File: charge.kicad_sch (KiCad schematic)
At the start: 2 parts, among them U1 BQ24640RVAR

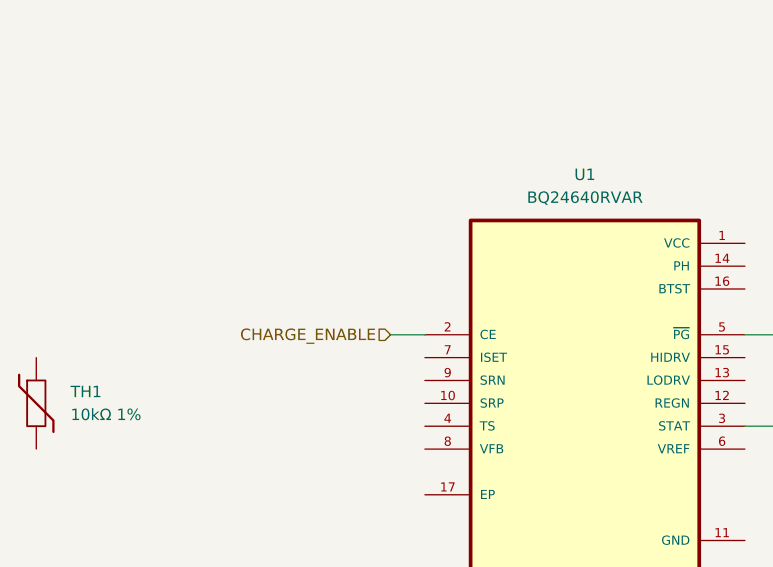
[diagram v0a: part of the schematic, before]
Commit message: Prefix all of the references so that the numbering is manageable across multiple circuits
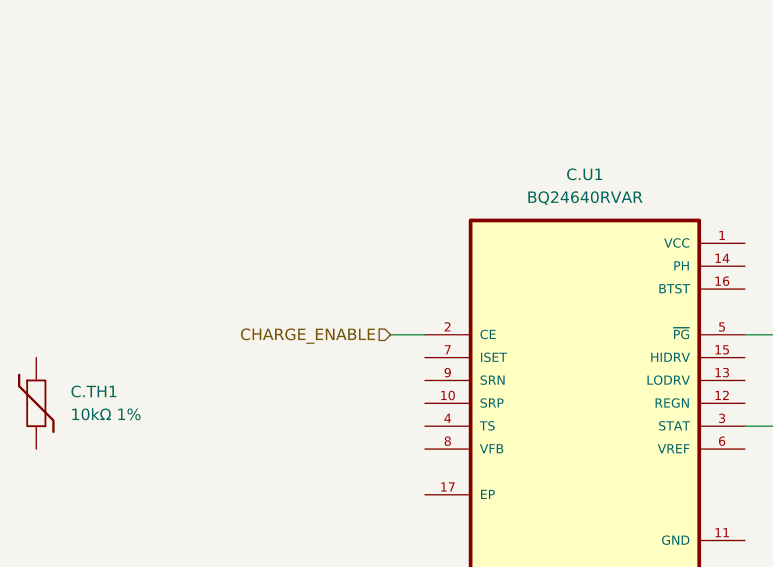
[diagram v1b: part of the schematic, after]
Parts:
- renumbered TH1 to C.TH1, U1 to C.U1
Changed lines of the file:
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@@
 		(dnp no)
 		(fields_autoplaced yes)
-		(property "Reference" "U1"
+		(property "Reference" "C.U1"
 			(at 74.93 39.37 0)
 			(effects
@@
 			(project ""
 				(path "/01e6e533-9ed1-4dde-bac5-1959ff8991e5/a1435003-e5d3-4de7-a692-f8e6f931526d"
-					(reference "U1")
+					(reference "C.U1")
 					(unit 1)
 				)
@@
 		(dnp no)
 		(fields_autoplaced yes)
-		(property "Reference" "TH1"
+		(property "Reference" "C.TH1"
 			(at 17.78 63.4999 0)
 			(effects
@@
 			(project "wireless-3v3-supercap"
 				(path "/01e6e533-9ed1-4dde-bac5-1959ff8991e5/a1435003-e5d3-4de7-a692-f8e6f931526d"
-					(reference "TH1")
+					(reference "C.TH1")
 					(unit 1)
 				)

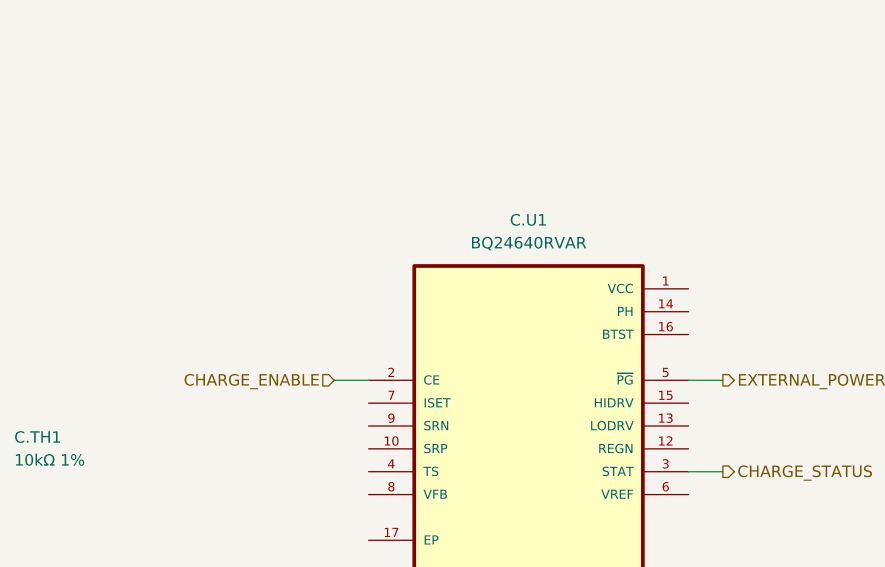
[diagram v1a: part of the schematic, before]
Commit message: Remove charge enable pin
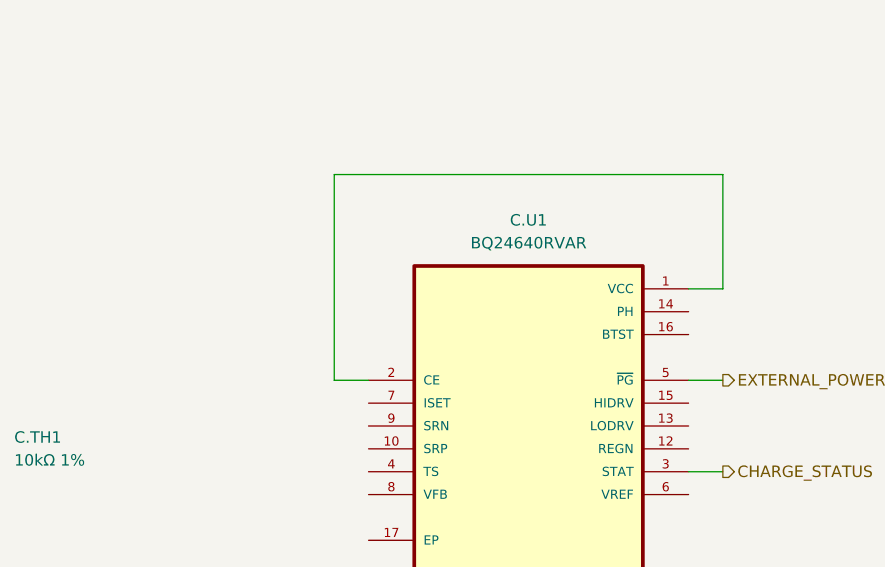
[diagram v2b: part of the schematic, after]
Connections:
- net CHARGE_ENABLE is gone; now on an unnamed net: C.U1.2 (CE)
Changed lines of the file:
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@@
+	(wire
+		(pts
+			(xy 53.34 34.29) (xy 96.52 34.29)
+		)
+		(stroke
+			(width 0)
+			(type default)
+		)
+	)
 	(wire
 		(pts
 			(xy 92.71 67.31) (xy 96.52 67.31)
+		)
+		(stroke
+			(width 0)
+			(type default)
+		)
+	)
+	(wire
+		(pts
+			(xy 96.52 46.99) (xy 92.71 46.99)
+		)
+		(stroke
+			(width 0)
+			(type default)
+		)
+	)
+	(wire
+		(pts
+			(xy 96.52 34.29) (xy 96.52 46.99)
+		)
+		(stroke
+			(width 0)
+			(type default)
+		)
+	)
+	(wire
+		(pts
+			(xy 53.34 57.15) (xy 53.34 34.29)
 		)
 		(stroke
@@
 		)
 	)
-	(hierarchical_label "CHARGE_ENABLE"
-		(shape input)
-		(at 53.34 57.15 180)
-		(effects
-			(font
-				(size 1.27 1.27)
-			)
-			(justify right)
-		)
-	)

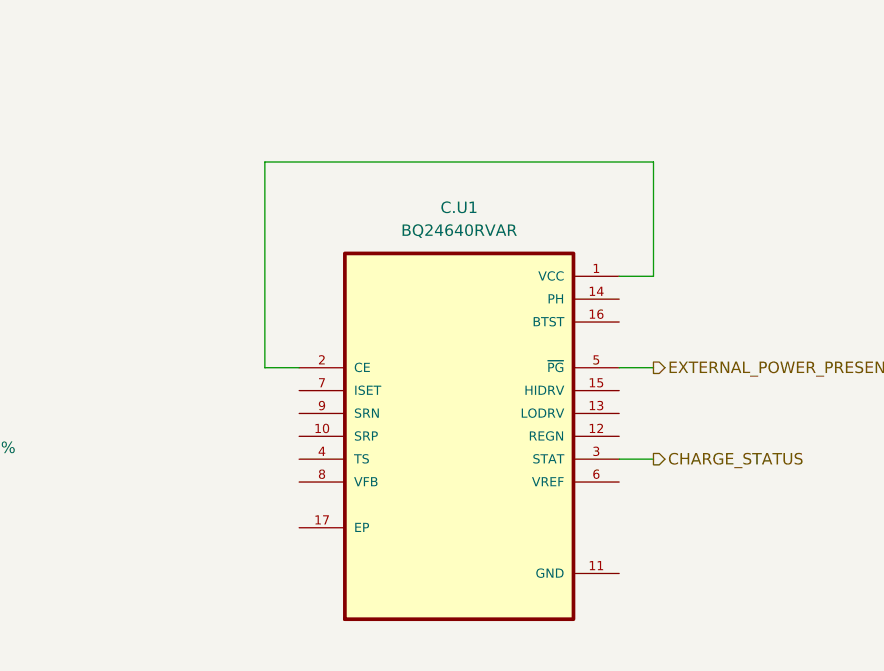
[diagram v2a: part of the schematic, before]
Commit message: Connect charger CE to VREF, not VCC
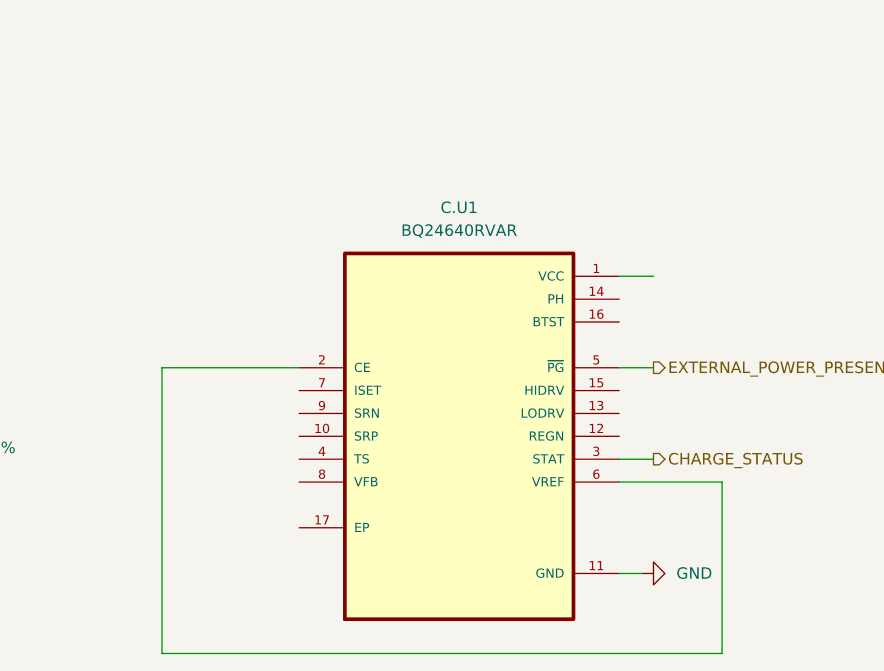
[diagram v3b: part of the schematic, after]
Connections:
- net at C.U1.1 (VCC): no longer C.U1.2 (CE)
- net GND: now reaches C.U1.11 (GND)
- net at C.U1.6 (VREF): now also C.U1.2 (CE)
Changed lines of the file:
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@@
 	(wire
 		(pts
-			(xy 53.34 34.29) (xy 96.52 34.29)
+			(xy 41.91 88.9) (xy 104.14 88.9)
+		)
+		(stroke
+			(width 0)
+			(type default)
+		)
+	)
+	(wire
+		(pts
+			(xy 104.14 69.85) (xy 92.71 69.85)
+		)
+		(stroke
+			(width 0)
+			(type default)
+		)
+	)
+	(wire
+		(pts
+			(xy 104.14 88.9) (xy 104.14 69.85)
 		)
 		(stroke
@@
 	(wire
 		(pts
+			(xy 41.91 57.15) (xy 41.91 88.9)
+		)
+		(stroke
+			(width 0)
+			(type default)
+		)
+	)
+	(wire
+		(pts
+			(xy 57.15 57.15) (xy 41.91 57.15)
+		)
+		(stroke
+			(width 0)
+			(type default)
+		)
+	)
+	(wire
+		(pts
 			(xy 96.52 46.99) (xy 92.71 46.99)
 		)
@@
 	(wire
 		(pts
-			(xy 96.52 34.29) (xy 96.52 46.99)
-		)
-		(stroke
-			(width 0)
-			(type default)
-		)
-	)
-	(wire
-		(pts
-			(xy 53.34 57.15) (xy 53.34 34.29)
-		)
-		(stroke
-			(width 0)
-			(type default)
-		)
-	)
-	(wire
-		(pts
-			(xy 53.34 57.15) (xy 57.15 57.15)
+			(xy 92.71 80.01) (xy 95.25 80.01)
 		)
 		(stroke
@@
 		)
 	)
+	(symbol
+		(lib_id "power:GND")
+		(at 95.25 80.01 90)
+		(unit 1)
+		(exclude_from_sim no)
+		(in_bom yes)
+		(on_board yes)
+		(dnp no)
+		(fields_autoplaced yes)
+		(property "Reference" "#PWR012"
+			(at 101.6 80.01 0)
+			(effects
+				(font
+					(size 1.27 1.27)
+				)
+				(hide yes)
+			)
+		)
+		(property "Value" "GND"
+			(at 99.06 80.0099 90)
+			(effects
+				(font
+					(size 1.27 1.27)
+				)
+				(justify right)
+			)
+		)
+		(property "Footprint" ""
+			(at 95.25 80.01 0)
+			(effects
+				(font
+					(size 1.27 1.27)
+				)
+				(hide yes)
+			)
+		)
+		(property "Datasheet" ""
+			(at 95.25 80.01 0)
+			(effects
+				(font
+					(size 1.27 1.27)
+				)
+				(hide yes)
+			)
+		)
+		(property "Description" "Power symbol creates a global label with name \"GND\" , ground"
+			(at 95.25 80.01 0)
+			(effects
+				(font
+					(size 1.27 1.27)
+				)
+				(hide yes)
+			)
+		)
+		(pin "1"
+		)
+		(instances
+			(project ""
+				(path "/01e6e533-9ed1-4dde-bac5-1959ff8991e5/a1435003-e5d3-4de7-a692-f8e6f931526d"
+					(reference "#PWR012")
+					(unit 1)
+				)
+			)
+		)
+	)

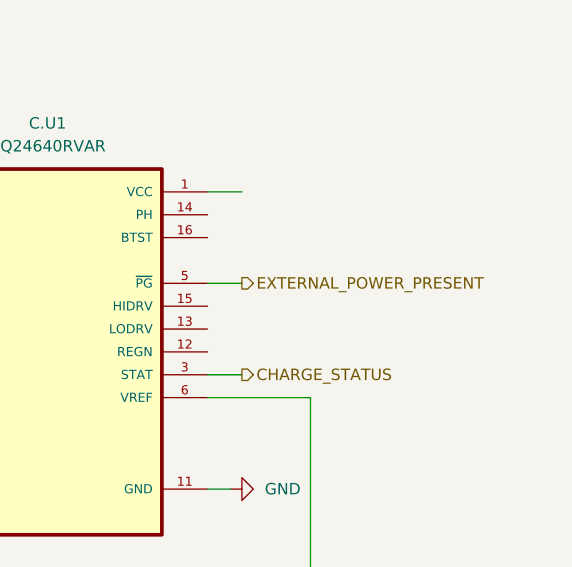
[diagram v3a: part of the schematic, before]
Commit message: Mark signals as active low
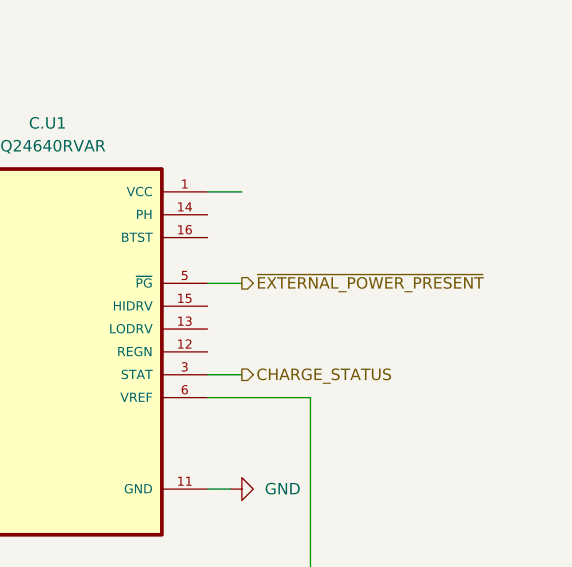
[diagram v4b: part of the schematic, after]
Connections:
- net EXTERNAL_POWER_PRESENT renamed ~{EXTERNAL_POWER_PRESENT}
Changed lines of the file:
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@@
 		)
 	)
-	(hierarchical_label "EXTERNAL_POWER_PRESENT"
+	(hierarchical_label "~{EXTERNAL_POWER_PRESENT}"
 		(shape output)
 		(at 96.52 57.15 0)

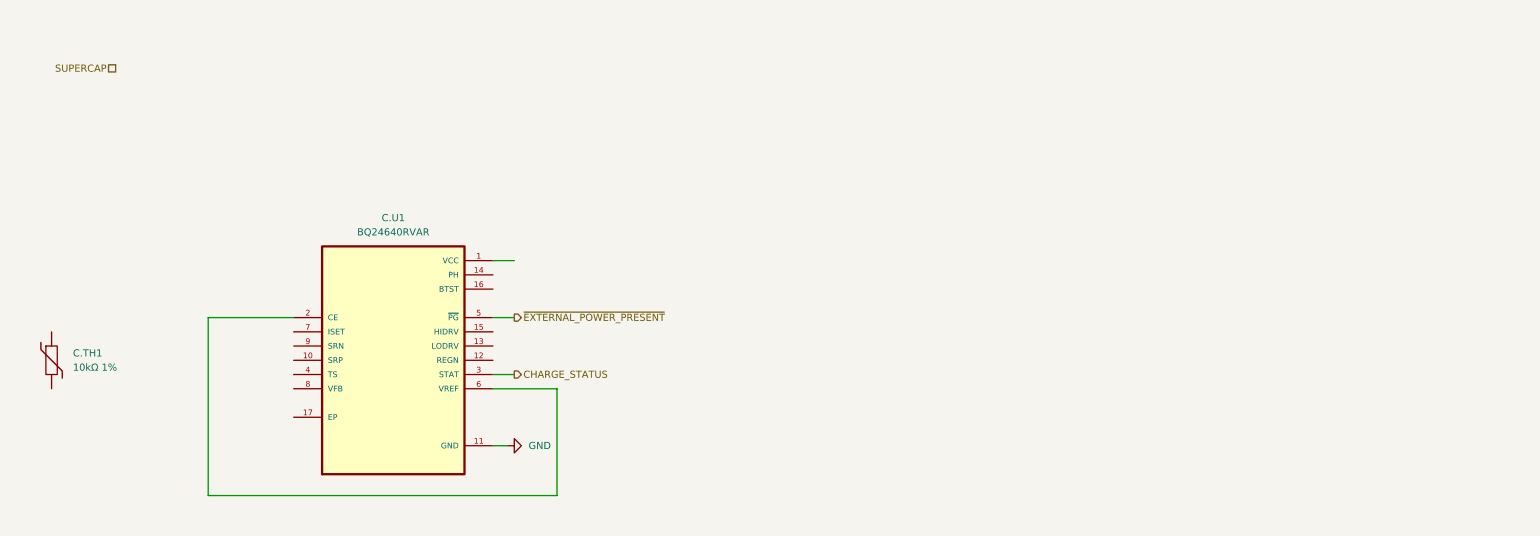
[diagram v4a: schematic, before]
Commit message: Add incomplete charge circuit
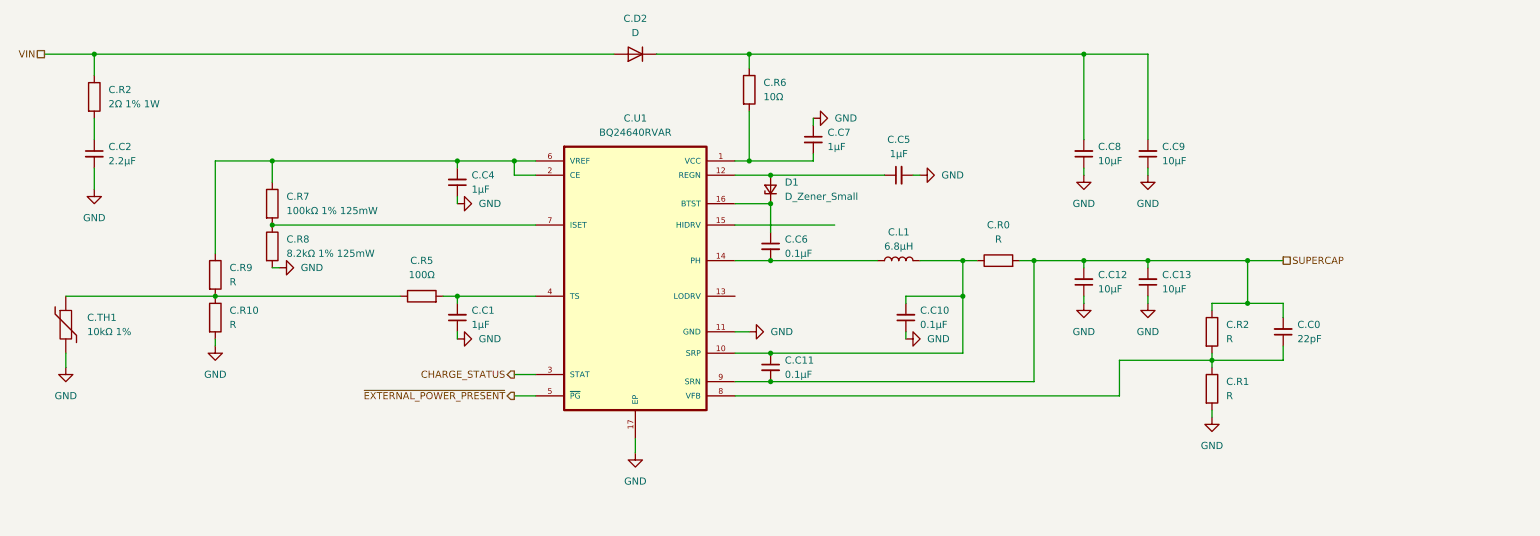
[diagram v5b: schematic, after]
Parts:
- added C.C0: 22pF, symbol Device:C_Small
- added C.C1, C.C4, C.C5, C.C7: 1µF, symbol Device:C_Small
- added C.C10, C.C11, C.C6: 0.1µF, symbol Device:C_Small
- added C.C12, C.C13, C.C8, C.C9: 10µF, symbol Device:C_Small
- added C.C2: 2.2µF, symbol Device:C_Small
- added C.D2: D, symbol Device:D
- added C.L1: 6.8µH, symbol Device:L
- added C.R0, C.R1, C.R10, C.R2, C.R9: R, symbol Device:R
- added C.R2: 2Ω 1% 1W, symbol Device:R
- added C.R5: 100Ω, symbol Device:R
- added C.R6: 10Ω, symbol Device:R
- added C.R7: 100kΩ 1% 125mW, symbol Device:R
- added C.R8: 8.2kΩ 1% 125mW, symbol Device:R
- added D1: D_Zener_Small, symbol Device:D_Zener_Small
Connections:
- net GND: now also C.TH1.2, C.U1.17 (EP), C.C1.1, C.C10.1, C.C12.1, C.C13.1, C.C2.2, C.C4.1, C.C5.2, C.C7.1, C.C8.1, C.C9.1, C.R1.2, C.R10.2, C.R8.2
- net SUPERCAP: now also C.U1.9 (SRN), C.C0.2, C.C11.2, C.C12.2, C.C13.2, C.R0.2, C.R2.1
- net at C.U1.1 (VCC): now also C.C7.2, C.R6.2
- net at C.U1.10 (SRP): now also C.C10.2, C.C11.1, C.L1.2, C.R0.1
- net at C.U1.12 (REGN): now also C.C5.1, D1.2 (A)
- net at C.U1.14 (PH): now also C.C6.2, C.L1.1
- net at C.U1.16 (BTST): now also C.C6.1, D1.1 (K)
- net at C.U1.2 (CE), C.U1.6 (VREF): now also C.C4.2, C.R7.1, C.R9.1
- net at C.U1.4 (TS): now also C.C1.2, C.R5.2
- net at C.U1.7 (ISET): now also C.R7.2, C.R8.1
- net at C.U1.8 (VFB): now also C.C0.1, C.R1.1, C.R2.2
- net at C.TH1.1: now also C.R10.1, C.R5.1, C.R9.2
- new net: C.C8.2, C.C9.2, C.D2.1 (K), C.R6.1
- new net: C.C2.1, C.R2.2
- new net VIN: C.D2.2 (A), C.R2.1
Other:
- moved on the sheet: C.TH1, C.U1

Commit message: Finish charge circuit
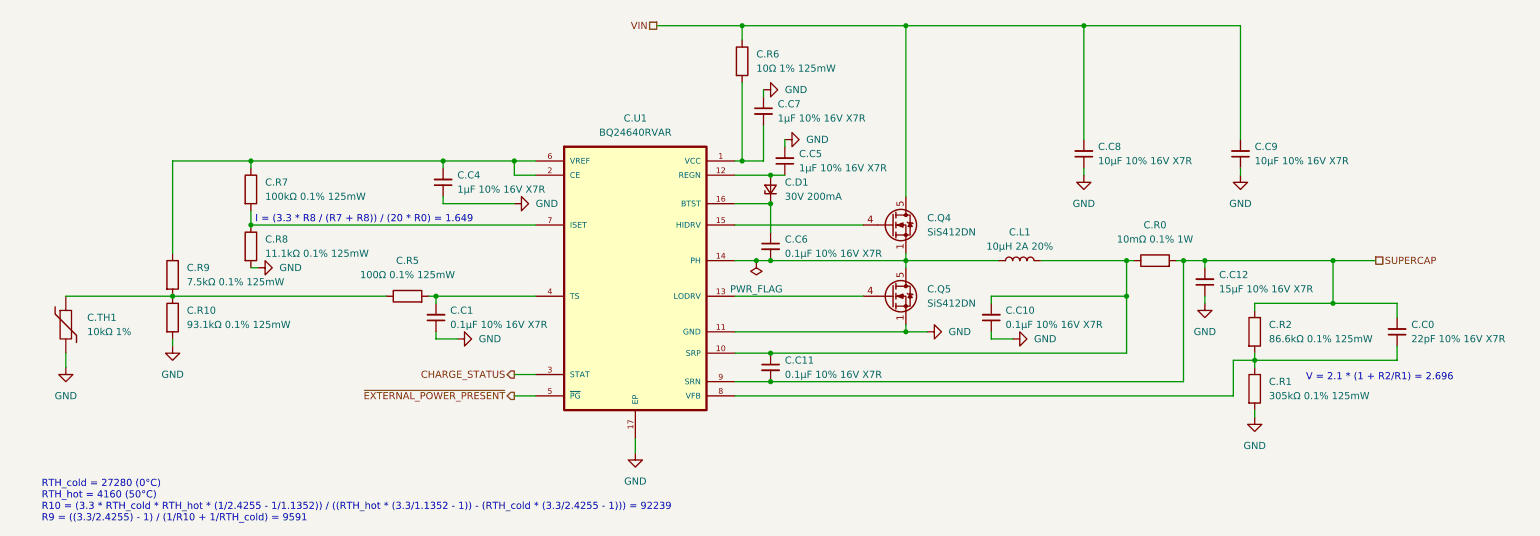
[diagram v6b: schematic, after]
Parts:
- removed C.C13: 10µF, symbol Device:C_Small
- removed C.C2: 2.2µF, symbol Device:C_Small
- removed C.D2: D, symbol Device:D
- removed C.R2: 2Ω 1% 1W, symbol Device:R
- added C.Q4, C.Q5: SiS412DN, Package_SO:Vishay_PowerPAK_1212-8_Single, symbol Transistor_FET:SiS454DN
- C.C0: value 22pF -> 22pF 10% 16V X7R; footprint (none) -> Capacitor_SMD:C_0805_2012Metric_Pad1.18x1.45mm_HandSolder
- C.C1: value 1µF -> 0.1µF 10% 16V X7R; footprint (none) -> Capacitor_SMD:C_0805_2012Metric_Pad1.18x1.45mm_HandSolder
- C.C10, C.C11, C.C6: value 0.1µF -> 0.1µF 10% 16V X7R; footprint (none) -> Capacitor_SMD:C_0805_2012Metric_Pad1.18x1.45mm_HandSolder
- C.C12: value 10µF -> 15µF 10% 16V X7R; footprint (none) -> Capacitor_SMD:C_1210_3225Metric_Pad1.33x2.70mm_HandSolder
- C.C4, C.C5, C.C7: value 1µF -> 1µF 10% 16V X7R; footprint (none) -> Capacitor_SMD:C_0805_2012Metric_Pad1.18x1.45mm_HandSolder
- C.C8, C.C9: value 10µF -> 10µF 10% 16V X7R; footprint (none) -> Capacitor_SMD:C_0805_2012Metric_Pad1.18x1.45mm_HandSolder
- C.D1: renamed from D1; value D_Zener_Small -> 30V 200mA; footprint (none) -> Package_TO_SOT_SMD:SOT-23-3
- C.L1: value 6.8µH -> 10µH 2A 20%; footprint (none) -> SRN5040:IND_SRN5040_BRN
- C.R0: value R -> 10mΩ 0.1% 1W; footprint (none) -> Resistor_SMD:R_0805_2012Metric_Pad1.20x1.40mm_HandSolder
- C.R1: value R -> 305kΩ 0.1% 125mW; footprint (none) -> Resistor_SMD:R_0805_2012Metric_Pad1.20x1.40mm_HandSolder
- C.R10: value R -> 93.1kΩ 0.1% 125mW; footprint (none) -> Resistor_SMD:R_0805_2012Metric_Pad1.20x1.40mm_HandSolder
- C.R2: value R -> 86.6kΩ 0.1% 125mW; footprint (none) -> Resistor_SMD:R_0805_2012Metric_Pad1.20x1.40mm_HandSolder
- C.R5: value 100Ω -> 100Ω 0.1% 125mW; footprint (none) -> Resistor_SMD:R_0805_2012Metric_Pad1.20x1.40mm_HandSolder
- C.R6: value 10Ω -> 10Ω 1% 125mW; footprint (none) -> Resistor_SMD:R_0805_2012Metric_Pad1.20x1.40mm_HandSolder
- C.R7: value 100kΩ 1% 125mW -> 100kΩ 0.1% 125mW; footprint (none) -> Resistor_SMD:R_0805_2012Metric_Pad1.20x1.40mm_HandSolder
- C.R8: value 8.2kΩ 1% 125mW -> 11.1kΩ 0.1% 125mW; footprint (none) -> Resistor_SMD:R_0805_2012Metric_Pad1.20x1.40mm_HandSolder
- C.R9: value R -> 7.5kΩ 0.1% 125mW; footprint (none) -> Resistor_SMD:R_0805_2012Metric_Pad1.20x1.40mm_HandSolder
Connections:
- net GND: now also C.Q5.1 (S), C.Q5.2 (S), C.Q5.3 (S)
- net VIN: now also C.C8.2, C.C9.2, C.R6.1, C.Q4.5 (D)
- net at C.C6.2, C.L1.1, C.U1.14 (PH): now also C.Q4.1 (S), C.Q4.2 (S), C.Q4.3 (S), C.Q5.5 (D)
- net at C.U1.13 (LODRV): now also C.Q5.4 (G)
- net at C.U1.15 (HIDRV): now also C.Q4.4 (G)
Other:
- note added: "I = (3.3 * R8 / (R7 + R8)) / (20 * R0) = 1.649"
- note added: "RTH_cold = 27280 (0°C) RTH_hot = 4160 (50°C) R10 = (3.3 * RTH_cold * RTH_hot * (1/2.4255 - 1/1.1352)) / ((RTH_hot * (3.3/1.1352 - 1)) - (RTH_cold * (3.3/2.4255 - 1))) = 92239 R9 = ((3.3/2.4255) - 1) / (1/R10 + 1/RTH_cold) = 9591"
- note added: "V = 2.1 * (1 + R2/R1) = 2.696"
- moved on the sheet: C.C0, C.C1, C.C10, C.C12, C.C4, C.C5, C.C7, C.C9, C.L1, C.R0, C.R1, C.R10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
